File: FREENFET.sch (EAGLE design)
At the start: 12 parts, among them IC1 WS2811-SOP8, Q1 RJU003N03, Q2 NTD5867NLT4G

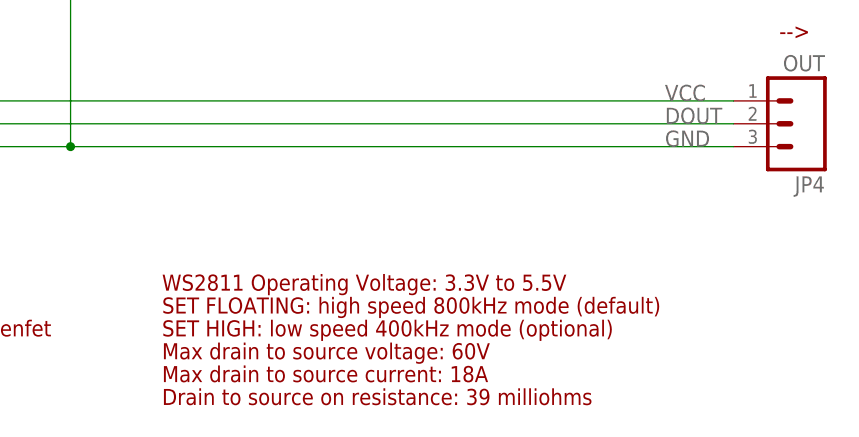
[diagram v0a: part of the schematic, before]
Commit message: Clarified schematic and silkscreen
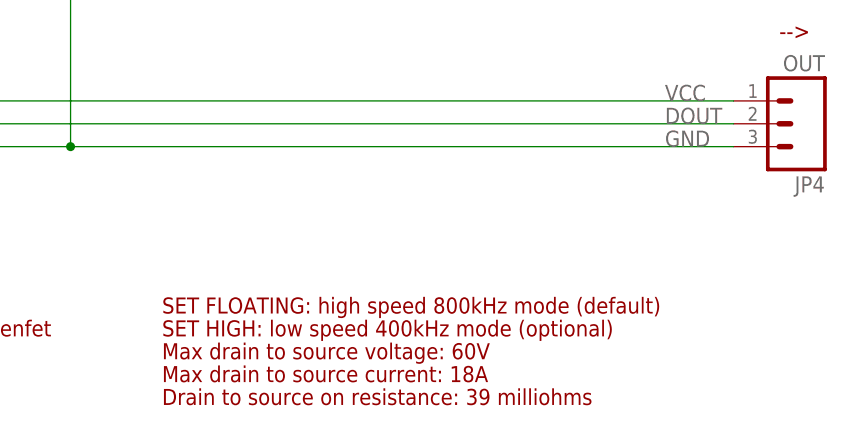
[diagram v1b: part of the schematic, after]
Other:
- note removed: "WS2811 Operating Voltage: 3.3V to 5.5V"
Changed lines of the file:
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@@
 <text x="7.366" y="6.35" size="1.778" layer="94">Released under the TAPR Open Hardware License: www.tapr.org/ohl</text>
 <text x="63.246" y="14.478" size="1.778" layer="94">www.freetronics.com.au/freenfet</text>
-<text x="111.76" y="19.558" size="1.778" layer="94">WS2811 Operating Voltage: 3.3V to 5.5V</text>
 <text x="7.62" y="47.498" size="1.778" layer="94">--&gt;</text>
 <text x="180.34" y="47.498" size="1.778" layer="94">--&gt;</text>

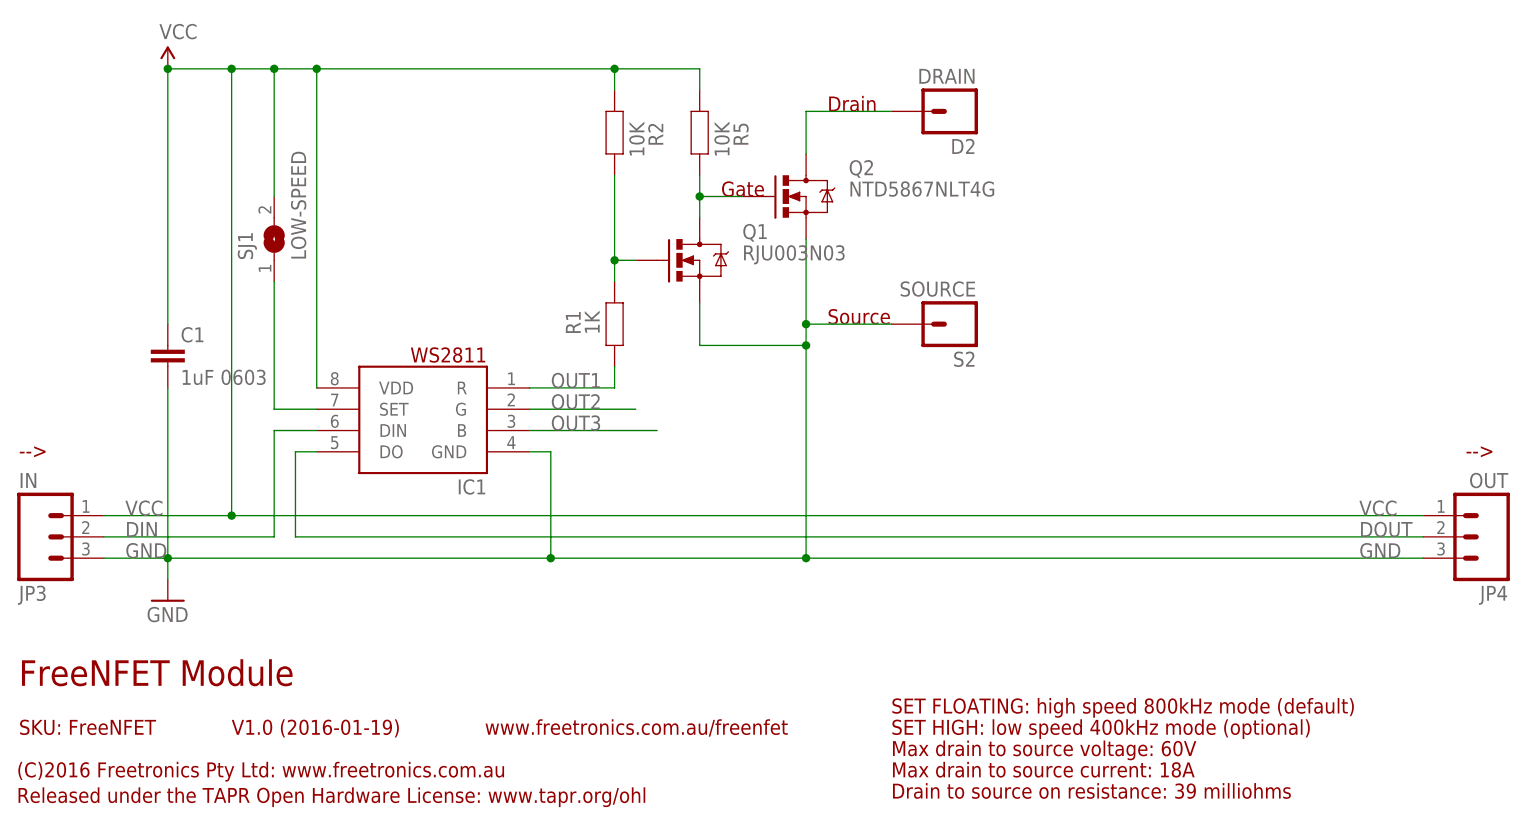
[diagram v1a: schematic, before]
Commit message: Designator improvement
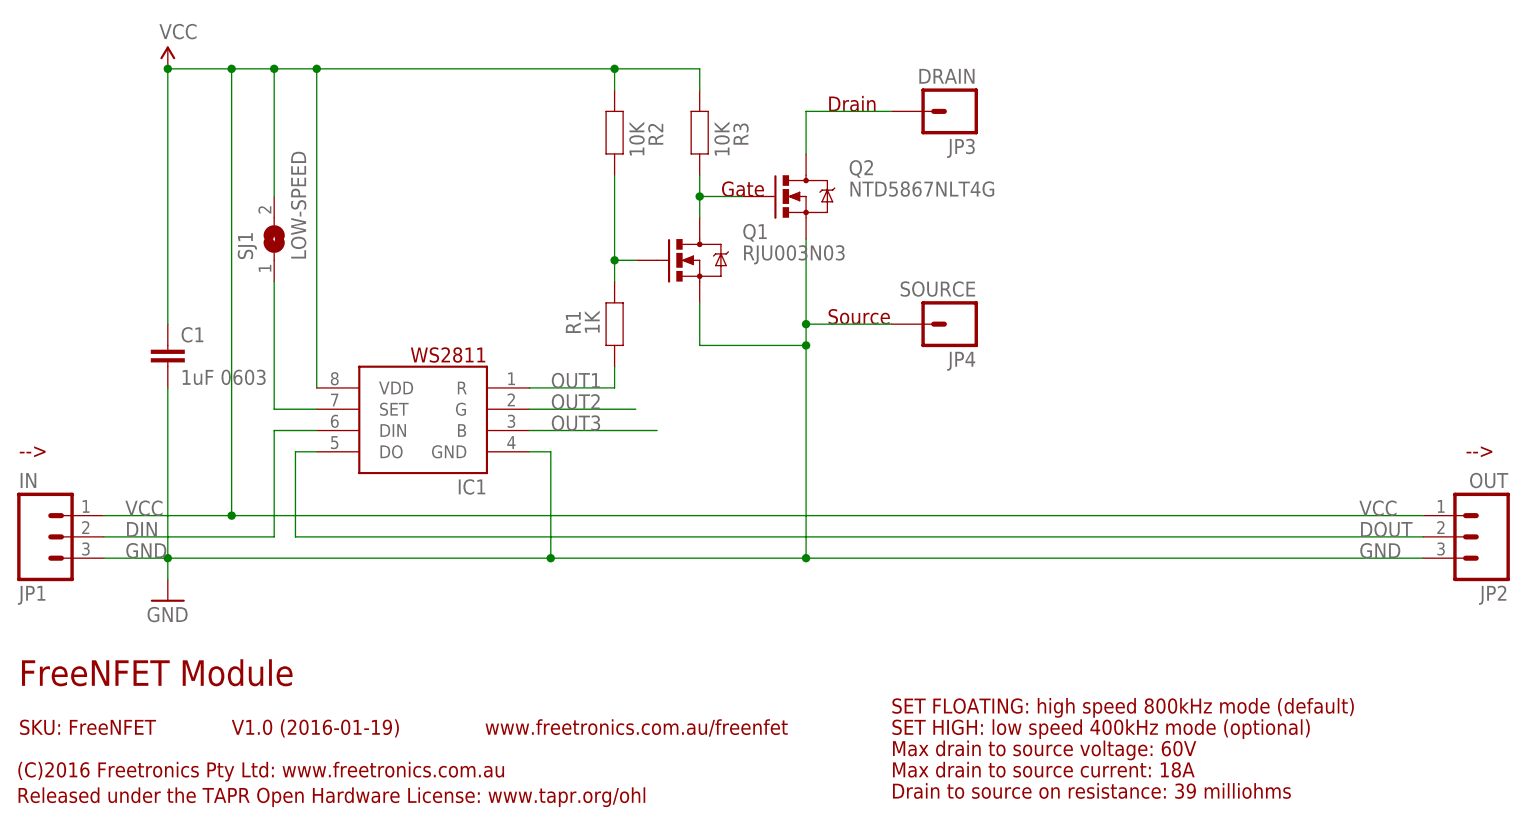
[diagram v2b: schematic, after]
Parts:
- removed D2: DRAIN, freetronics-master-v1.1:M01PTH_LARGE
- removed S2: SOURCE, freetronics-master-v1.1:M01PTH_LARGE
- added JP1: IN, freetronics-jon:M03PTH
- added JP2: OUT, freetronics-jon:M03PTH
- JP3: value IN -> DRAIN; device freetronics-jon:M03PTH -> freetronics-master-v1.1:M01PTH_LARGE
- JP4: value OUT -> SOURCE; device freetronics-jon:M03PTH -> freetronics-master-v1.1:M01PTH_LARGE
- renumbered R5 to R3
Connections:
- net D: now also JP3.1; no longer D2.1
- net DIN: now also JP1.2; no longer JP3.2
- net DOUT: now also JP2.2; no longer JP4.2
- net GND: now also JP1.3, JP2.3, JP4.1; no longer JP3.3, JP4.3, S2.1
- net VCC: now also JP1.1, JP2.1; no longer JP3.1, JP4.1
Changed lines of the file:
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@@
 <part name="C1" library="freetronics-master-v1" deviceset="CAP" device="0603" value="1uF 0603"/>
 <part name="Q2" library="freetronics-master-v1.1" deviceset="MOSFET-NCHANNEL" device="DPAK" value="NTD5867NLT4G"/>
-<part name="R5" library="freetronics-master-v1" deviceset="RESISTOR" device="0603" value="10K"/>
-<part name="D2" library="freetronics-master-v1.1" deviceset="M01" device="PTH_LARGE" value="DRAIN"/>
-<part name="S2" library="freetronics-master-v1.1" deviceset="M01" device="PTH_LARGE" value="SOURCE"/>
+<part name="R3" library="freetronics-master-v1" deviceset="RESISTOR" device="0603" value="10K"/>
+<part name="JP3" library="freetronics-master-v1.1" deviceset="M01" device="PTH_LARGE" value="DRAIN"/>
+<part name="JP4" library="freetronics-master-v1.1" deviceset="M01" device="PTH_LARGE" value="SOURCE"/>
 <part name="IC1" library="freetronics-jon" deviceset="WS2811" device="-SOP8"/>
-<part name="JP3" library="freetronics-jon" deviceset="M03" device="PTH" value="IN"/>
-<part name="JP4" library="freetronics-jon" deviceset="M03" device="PTH" value="OUT"/>
+<part name="JP1" library="freetronics-jon" deviceset="M03" device="PTH" value="IN"/>
+<part name="JP2" library="freetronics-jon" deviceset="M03" device="PTH" value="OUT"/>
 <part name="GND2" library="freetronics" deviceset="GND" device=""/>
 <part name="Q1" library="freetronics-jon" deviceset="MOSFET-N" device="SOT-323" value="RJU003N03"/>
@@
 <instance part="C1" gate="G$1" x="25.4" y="58.42"/>
 <instance part="Q2" gate="G$1" x="101.6" y="78.74"/>
-<instance part="R5" gate="G$1" x="88.9" y="86.36" smashed="yes" rot="R90">
+<instance part="R3" gate="G$1" x="88.9" y="86.36" smashed="yes" rot="R90">
 <attribute name="NAME" x="92.9386" y="87.63" size="1.778" layer="95" rot="R270"/>
 <attribute name="VALUE" x="90.678" y="87.63" size="1.778" layer="96" rot="R270"/>
 </instance>
-<instance part="D2" gate="G$1" x="119.38" y="88.9" rot="R180"/>
-<instance part="S2" gate="G$1" x="119.38" y="63.5" rot="R180"/>
+<instance part="JP3" gate="G$1" x="119.38" y="88.9" rot="R180"/>
+<instance part="JP4" gate="G$1" x="119.38" y="63.5" rot="R180"/>
 <instance part="IC1" gate="G$1" x="55.88" y="50.8" rot="MR0"/>
-<instance part="JP3" gate="G$1" x="10.16" y="38.1" rot="MR180"/>
-<instance part="JP4" gate="G$1" x="182.88" y="38.1" rot="R180"/>
+<instance part="JP1" gate="G$1" x="10.16" y="38.1" rot="MR180"/>
+<instance part="JP2" gate="G$1" x="182.88" y="38.1" rot="R180"/>
 <instance part="GND2" gate="1" x="25.4" y="30.48"/>
 <instance part="Q1" gate="G$1" x="88.9" y="71.12"/>
@@
 <wire x1="101.6" y1="73.66" x2="101.6" y2="63.5" width="0.1524" layer="91"/>
 <pinref part="Q2" gate="G$1" pin="S"/>
-<pinref part="S2" gate="G$1" pin="1"/>
+<pinref part="JP4" gate="G$1" pin="1"/>
 <pinref part="Q1" gate="G$1" pin="S"/>
 <wire x1="88.9" y1="60.96" x2="101.6" y2="60.96" width="0.1524" layer="91"/>
@@
 <junction x="25.4" y="35.56"/>
 <label x="20.32" y="35.56" size="1.778" layer="95"/>
-<pinref part="JP3" gate="G$1" pin="3"/>
+<pinref part="JP1" gate="G$1" pin="3"/>
 <wire x1="25.4" y1="35.56" x2="71.12" y2="35.56" width="0.1524" layer="91"/>
-<pinref part="JP4" gate="G$1" pin="3"/>
+<pinref part="JP2" gate="G$1" pin="3"/>
 <pinref part="GND2" gate="1" pin="GND"/>
 <wire x1="71.12" y1="35.56" x2="101.6" y2="35.56" width="0.1524" layer="91"/>
@@
 <net name="VCC" class="0">
 <segment>
-<pinref part="R5" gate="G$1" pin="2"/>
+<pinref part="R3" gate="G$1" pin="2"/>
 <wire x1="88.9" y1="93.98" x2="88.9" y2="91.44" width="0.1524" layer="91"/>
 <pinref part="R2" gate="G$1" pin="2"/>
@@
 <pinref part="C1" gate="G$1" pin="1"/>
 <label x="20.32" y="40.64" size="1.778" layer="95"/>
-<pinref part="JP3" gate="G$1" pin="1"/>
-<pinref part="JP4" gate="G$1" pin="1"/>
+<pinref part="JP1" gate="G$1" pin="1"/>
+<pinref part="JP2" gate="G$1" pin="1"/>
 <wire x1="17.78" y1="40.64" x2="33.02" y2="40.64" width="0.1524" layer="91"/>
 <wire x1="33.02" y1="40.64" x2="175.26" y2="40.64" width="0.1524" layer="91"/>
@@
 <wire x1="101.6" y1="88.9" x2="111.76" y2="88.9" width="0.1524" layer="91"/>
 <pinref part="Q2" gate="G$1" pin="D"/>
-<pinref part="D2" gate="G$1" pin="1"/>
+<pinref part="JP3" gate="G$1" pin="1"/>
 </segment>
 </net>
@@
 <wire x1="88.9" y1="81.28" x2="88.9" y2="78.74" width="0.1524" layer="91"/>
 <pinref part="Q2" gate="G$1" pin="G"/>
-<pinref part="R5" gate="G$1" pin="1"/>
+<pinref part="R3" gate="G$1" pin="1"/>
 <pinref part="Q1" gate="G$1" pin="D"/>
 <wire x1="88.9" y1="78.74" x2="93.98" y2="78.74" width="0.1524" layer="91"/>
@@
 <segment>
 <pinref part="IC1" gate="G$1" pin="DIN"/>
-<pinref part="JP3" gate="G$1" pin="2"/>
+<pinref part="JP1" gate="G$1" pin="2"/>
 <wire x1="43.18" y1="50.8" x2="38.1" y2="50.8" width="0.1524" layer="91"/>
 <wire x1="38.1" y1="50.8" x2="38.1" y2="38.1" width="0.1524" layer="91"/>
@@
 <wire x1="43.18" y1="48.26" x2="40.64" y2="48.26" width="0.1524" layer="91"/>
 <wire x1="40.64" y1="48.26" x2="40.64" y2="38.1" width="0.1524" layer="91"/>
-<pinref part="JP4" gate="G$1" pin="2"/>
+<pinref part="JP2" gate="G$1" pin="2"/>
 <wire x1="40.64" y1="38.1" x2="175.26" y2="38.1" width="0.1524" layer="91"/>
 <label x="167.64" y="38.1" size="1.778" layer="95"/>
